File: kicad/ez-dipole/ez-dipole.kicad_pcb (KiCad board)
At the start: 2 copper layers, 200 x 80 mm, 4 parts, among them J1 Conn_Coaxial

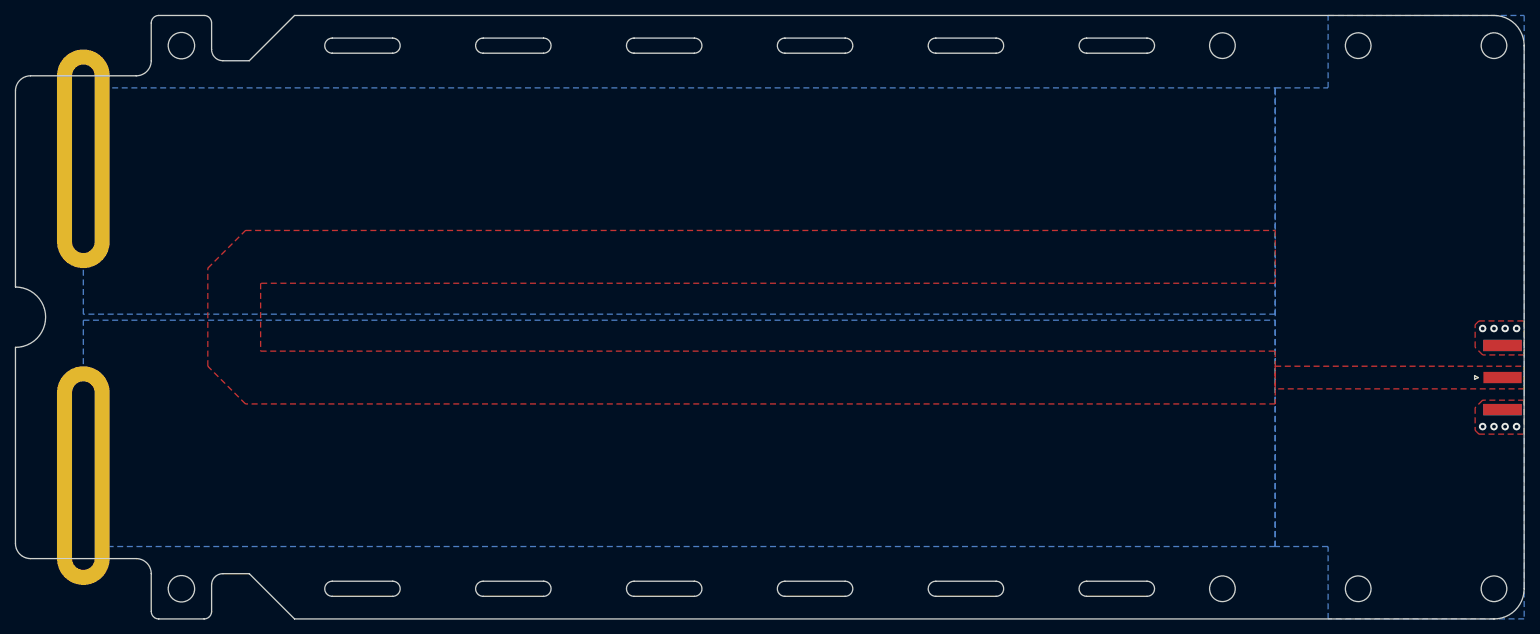
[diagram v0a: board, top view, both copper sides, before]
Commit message: Increased slot length outside of board outline and adapted SMA footprint to allow also smaller SMA connectors
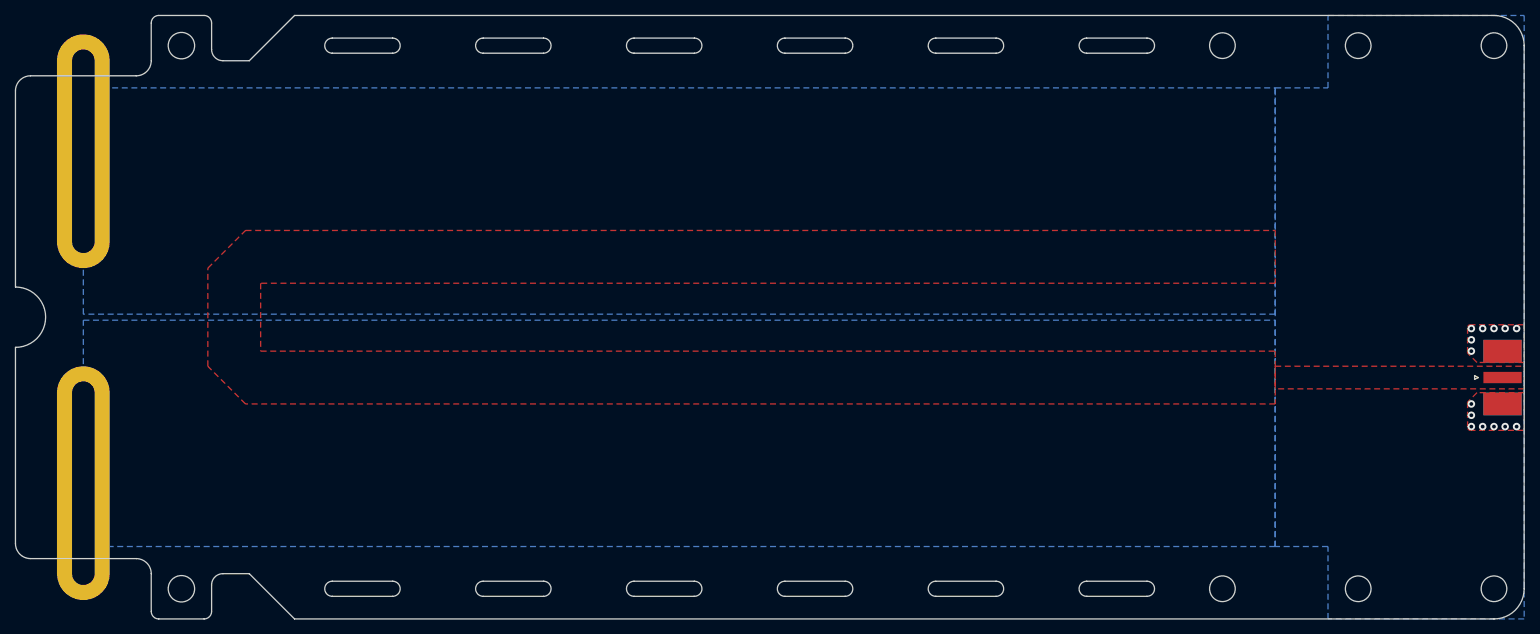
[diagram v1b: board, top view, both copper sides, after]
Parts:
- J1: footprint Connector_Coaxial:SMA_Amphenol_132289_EdgeMount -> ez-dipole:SMA_Amphenol_132289_EdgeMount
- moved TP1 1.00 mm to (60.0, 68.0)
- moved TP2 1.00 mm to (60.0, 112.0)
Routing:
- net GND: vias 8 -> 14
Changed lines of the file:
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@@
   (net 2 "/HOT")
   (footprint "ez-dipole:Slot" (layer "F.Cu")
-    (at 60 111 90)
+    (at 60 112 90)
     (property "Sheetfile" "ez-dipole.kicad_sch")
     (property "Sheetname" "")
@@
       (effects (font (size 1 1) (thickness 0.15)))
     )
-    (pad "1" thru_hole oval (at 0 0 90) (size 29 7) (drill oval 25 3) (layers *.Cu *.Mask)
+    (pad "1" thru_hole oval (at 0 0 90) (size 31 7) (drill oval 27 3) (layers *.Cu *.Mask)
       (net 1 "GND") (pinfunction "1") (pintype "passive"))
   )
-  (footprint "Connector_Coaxial:SMA_Amphenol_132289_EdgeMount" (layer "F.Cu")
+  (footprint "ez-dipole:SMA_Amphenol_132289_EdgeMount" locked (layer "F.Cu")
     (at 248.1375 98)
     (descr "http://www.amphenolrf.com/132289.html")
@@
       (effects (font (size 1 1) (thickness 0.15)))
     )
-    (fp_text value "Conn_Coaxial" (at 5 6) (layer "F.Fab") hide
+    (fp_text value "Conn_Coaxial" (at 5 6) (layer "F.Fab")
       (effects (font (size 1 1) (thickness 0.15)))
     )
-    (fp_text user "${REFERENCE}" (at 4.79 0 270) (layer "F.Fab") hide
+    (fp_text user "${REFERENCE}" (at 4.79 0 270) (layer "F.Fab")
       (effects (font (size 1 1) (thickness 0.15)))
     )
+    (fp_line (start -3.71 0.25) (end -3.21 0) (layer "F.SilkS") (width 0.12))
+    (fp_line (start -3.21 0) (end -3.71 -0.25) (layer "F.SilkS") (width 0.12))
     (fp_line (start -3.71 -0.25) (end -3.71 0.25) (layer "F.SilkS") (width 0.12))
-    (fp_line (start -3.21 0) (end -3.71 -0.25) (layer "F.SilkS") (width 0.12))
-    (fp_line (start -3.71 0.25) (end -3.21 0) (layer "F.SilkS") (width 0.12))
-    (fp_line (start 14.47 -5.58) (end -3.04 -5.58) (layer "B.CrtYd") (width 0.05))
+    (fp_line (start -3.04 5.58) (end -3.04 -5.58) (layer "B.CrtYd") (width 0.05))
     (fp_line (start 14.47 -5.58) (end 14.47 5.58) (layer "B.CrtYd") (width 0.05))
     (fp_line (start 14.47 5.58) (end -3.04 5.58) (layer "B.CrtYd") (width 0.05))
-    (fp_line (start -3.04 5.58) (end -3.04 -5.58) (layer "B.CrtYd") (width 0.05))
+    (fp_line (start 14.47 -5.58) (end -3.04 -5.58) (layer "B.CrtYd") (width 0.05))
     (fp_line (start 14.47 5.58) (end -3.04 5.58) (layer "F.CrtYd") (width 0.05))
     (fp_line (start 14.47 -5.58) (end 14.47 5.58) (layer "F.CrtYd") (width 0.05))
@@
     (fp_line (start 14.47 -5.58) (end -3.04 -5.58) (layer "F.CrtYd") (width 0.05))
     (fp_line (start 2.54 3.81) (end -1.91 3.81) (layer "F.Fab") (width 0.1))
-    (fp_line (start 2.54 -3.81) (end 2.54 3.81) (layer "F.Fab") (width 0.1))
-    (fp_line (start -1.91 -5.08) (end 4.445 -5.08) (layer "F.Fab") (width 0.1))
     (fp_line (start 4.445 -3.81) (end 13.97 -3.81) (layer "F.Fab") (width 0.1))
     (fp_line (start 3.54 0) (end 2.54 0.75) (layer "F.Fab") (width 0.1))
+    (fp_line (start 13.97 -3.81) (end 13.97 3.81) (layer "F.Fab") (width 0.1))
+    (fp_line (start 4.445 5.08) (end 4.445 3.81) (layer "F.Fab") (width 0.1))
+    (fp_line (start 2.54 -3.81) (end 2.54 3.81) (layer "F.Fab") (width 0.1))
     (fp_line (start -1.91 3.81) (end -1.91 5.08) (layer "F.Fab") (width 0.1))
+    (fp_line (start -1.91 -5.08) (end 4.445 -5.08) (layer "F.Fab") (width 0.1))
+    (fp_line (start 2.54 -0.75) (end 3.54 0) (layer "F.Fab") (width 0.1))
+    (fp_line (start -1.91 -3.81) (end 2.54 -3.81) (layer "F.Fab") (width 0.1))
     (fp_line (start -1.91 -5.08) (end -1.91 -3.81) (layer "F.Fab") (width 0.1))
+    (fp_line (start -1.91 5.08) (end 4.445 5.08) (layer "F.Fab") (width 0.1))
+    (fp_line (start 4.445 -3.81) (end 4.445 -5.08) (layer "F.Fab") (width 0.1))
     (fp_line (start 13.97 3.81) (end 4.445 3.81) (layer "F.Fab") (width 0.1))
-    (fp_line (start 2.54 -0.75) (end 3.54 0) (layer "F.Fab") (width 0.1))
-    (fp_line (start 4.445 -3.81) (end 4.445 -5.08) (layer "F.Fab") (width 0.1))
-    (fp_line (start -1.91 -3.81) (end 2.54 -3.81) (layer "F.Fab") (width 0.1))
-    (fp_line (start 4.445 5.08) (end 4.445 3.81) (layer "F.Fab") (width 0.1))
-    (fp_line (start -1.91 5.08) (end 4.445 5.08) (layer "F.Fab") (width 0.1))
-    (fp_line (start 13.97 -3.81) (end 13.97 3.81) (layer "F.Fab") (width 0.1))
-    (pad "1" smd rect (at 0 0 90) (size 1.5 5.08) (layers "F.Cu" "F.Paste" "F.Mask")
+    (pad "1" smd rect locked (at 0 0 90) (size 1.5 5.08) (layers "F.Cu" "F.Paste" "F.Mask")
       (net 2 "/HOT") (pinfunction "In") (pintype "passive"))
-    (pad "2" smd rect (at 0 4.25 90) (size 1.5 5.08) (layers "B.Cu" "B.Paste" "B.Mask")
+    (pad "2" smd rect locked (at 0 3.5 90) (size 3 5.08) (layers "F.Cu" "F.Paste" "F.Mask")
       (net 1 "GND") (pinfunction "Ext") (pintype "passive"))
-    (pad "2" smd rect (at 0 4.25 90) (size 1.5 5.08) (layers "F.Cu" "F.Paste" "F.Mask")
+    (pad "2" smd rect locked (at 0 -3.5 90) (size 3 5.08) (layers "B.Cu" "B.Paste" "B.Mask")
       (net 1 "GND") (pinfunction "Ext") (pintype "passive"))
-    (pad "2" smd rect (at 0 -4.25 90) (size 1.5 5.08) (layers "B.Cu" "B.Paste" "B.Mask")
+    (pad "2" smd rect locked (at 0 -3.5 90) (size 3 5.08) (layers "F.Cu" "F.Paste" "F.Mask")
       (net 1 "GND") (pinfunction "Ext") (pintype "passive"))
-    (pad "2" smd rect (at 0 -4.25 90) (size 1.5 5.08) (layers "F.Cu" "F.Paste" "F.Mask")
+    (pad "2" smd rect locked (at 0 3.5 90) (size 3 5.08) (layers "B.Cu" "B.Paste" "B.Mask")
       (net 1 "GND") (pinfunction "Ext") (pintype "passive"))
     (model "${KIPRJMOD}/../library/ez-dipole.3dshapes/SMA_Amphenol_132289_EdgeMount.stp"
-      (offset (xyz 2.9 0 0.4))
+      (offset (xyz 2.5 0 0.35))
       (scale (xyz 1 1 1))
-      (rotate (xyz 90 -180 0))
+      (rotate (xyz -90 0 180))
     )
   )
   (footprint "ez-dipole:Slot" (layer "F.Cu")
-    (at 60 69 90)
+    (at 60 68 90)
     (property "Sheetfile" "ez-dipole.kicad_sch")
     (property "Sheetname" "")
@@
       (effects (font (size 1 1) (thickness 0.15)))
     )
-    (pad "1" thru_hole oval (at 0 0 90) (size 29 7) (drill oval 25 3) (layers *.Cu *.Mask)
+    (pad "1" thru_hole oval (at 0 0 90) (size 31 7) (drill oval 27 3) (layers *.Cu *.Mask)
       (net 1 "GND") (pinfunction "1") (pintype "passive"))
   )
@@
   (gr_rect (start 251 130) (end 51 122) (layer "B.Mask") (width 0.15) (fill solid))
   (gr_rect (start 251 58) (end 51 50) (layer "F.Mask") (width 0.15) (fill solid))
+  (gr_rect (start 250.7 93) (end 245.6 96) (layer "F.Mask") (width 0.1) (fill solid))
+  (gr_rect (start 245.6 103) (end 250.7 100) (layer "F.Mask") (width 0.1) (fill solid))
   (gr_rect (start 251 130) (end 51 122) (layer "F.Mask") (width 0.15) (fill solid))
   (gr_line (start 250 90) (end 50 90) (layer "Dwgs.User") (width 0.15))
@@
   )
   (via (at 247 91.5) (size 1) (drill 0.5) (layers "F.Cu" "B.Cu") (free) (net 1))
+  (via (at 248.478731 104.501145) (size 1) (drill 0.5) (layers "F.Cu" "B.Cu") (free) (net 1))
+  (via (at 250 104.5) (size 1) (drill 0.5) (layers "F.Cu" "B.Cu") (free) (net 1))
+  (via (at 244 104.5) (size 1) (drill 0.5) (layers "F.Cu" "B.Cu") (free) (net 1))
   (via (at 250 91.5) (size 1) (drill 0.5) (layers "F.Cu" "B.Cu") (free) (net 1))
-  (via (at 250 104.5) (size 1) (drill 0.5) (layers "F.Cu" "B.Cu") (free) (net 1))
+  (via (at 245.5 104.5) (size 1) (drill 0.5) (layers "F.Cu" "B.Cu") (free) (net 1))
   (via (at 248.478731 91.498855) (size 1) (drill 0.5) (layers "F.Cu" "B.Cu") (free) (net 1))
+  (via (at 244 91.5) (size 1) (drill 0.5) (layers "F.Cu" "B.Cu") (free) (net 1))
+  (via (at 244 103) (size 1) (drill 0.5) (layers "F.Cu" "B.Cu") (free) (net 1))
+  (via (at 244 93) (size 1) (drill 0.5) (layers "F.Cu" "B.Cu") (free) (net 1))
   (via (at 247 104.5) (size 1) (drill 0.5) (layers "F.Cu" "B.Cu") (free) (net 1))
-  (via (at 248.478731 104.501145) (size 1) (drill 0.5) (layers "F.Cu" "B.Cu") (free) (net 1))
+  (via (at 244 94.5) (size 1) (drill 0.5) (layers "F.Cu" "B.Cu") (free) (net 1))
   (via (at 245.5 91.5) (size 1) (drill 0.5) (layers "F.Cu" "B.Cu") (free) (net 1))
-  (via (at 245.5 104.5) (size 1) (drill 0.5) (layers "F.Cu" "B.Cu") (free) (net 1))
+  (via (at 244 101.5) (size 1) (drill 0.5) (layers "F.Cu" "B.Cu") (free) (net 1))
   (zone (net 2) (net_name "/HOT") (layer "F.Cu") (hatch edge 0.508)
     (connect_pads yes (clearance 0.508))
@@
     )
   )
+  (zone (net 1) (net_name "GND") (layer "F.Cu") (hatch edge 0.508)
+    (connect_pads yes (clearance 0.3))
+    (min_thickness 0.254) (filled_areas_thickness no)
+    (fill yes (thermal_gap 0.508) (thermal_bridge_width 0.508) (island_removal_mode 1) (island_area_min 0))
+    (polygon
+      (pts
+        (xy 251 100)
+        (xy 244.75 100)
+        (xy 243.5 101.25)
+        (xy 243.5 104.75)
+        (xy 243.75 105)
+        (xy 251 105)
+      )
+    )
+  )
   (zone (net 2) (net_name "/HOT") (layer "F.Cu") (hatch edge 0.508)
     (connect_pads yes (clearance 0.3))
@@
     (polygon
       (pts
-        (xy 251 95)
-        (xy 245.5 95)
-        (xy 244.5 94)
-        (xy 244.5 91)
-        (xy 245 90.5)
-        (xy 251 90.5)
+        (xy 251 96)
+        (xy 244.75 96)
+        (xy 243.5 94.75)
+        (xy 243.5 91.25)
+        (xy 243.75 91)
+        (xy 251 91)
       )
     )
-  )
-  (zone (net 1) (net_name "GND") (layer "F.Cu") (hatch edge 0.508)
-    (connect_pads yes (clearance 0.3))
-    (min_thickness 0.254) (filled_areas_thickness no)
-    (fill yes (thermal_gap 0.508) (thermal_bridge_width 0.508) (island_removal_mode 1) (island_area_min 0))
-    (polygon
-      (pts
-        (xy 251 101)
-        (xy 245.5 101)
-        (xy 244.5 102)
-        (xy 244.5 105)
-        (xy 245 105.5)
-        (xy 251 105.5)
-      )
-    )

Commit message: Updated PCB to revision 1.1 with updated simulation data
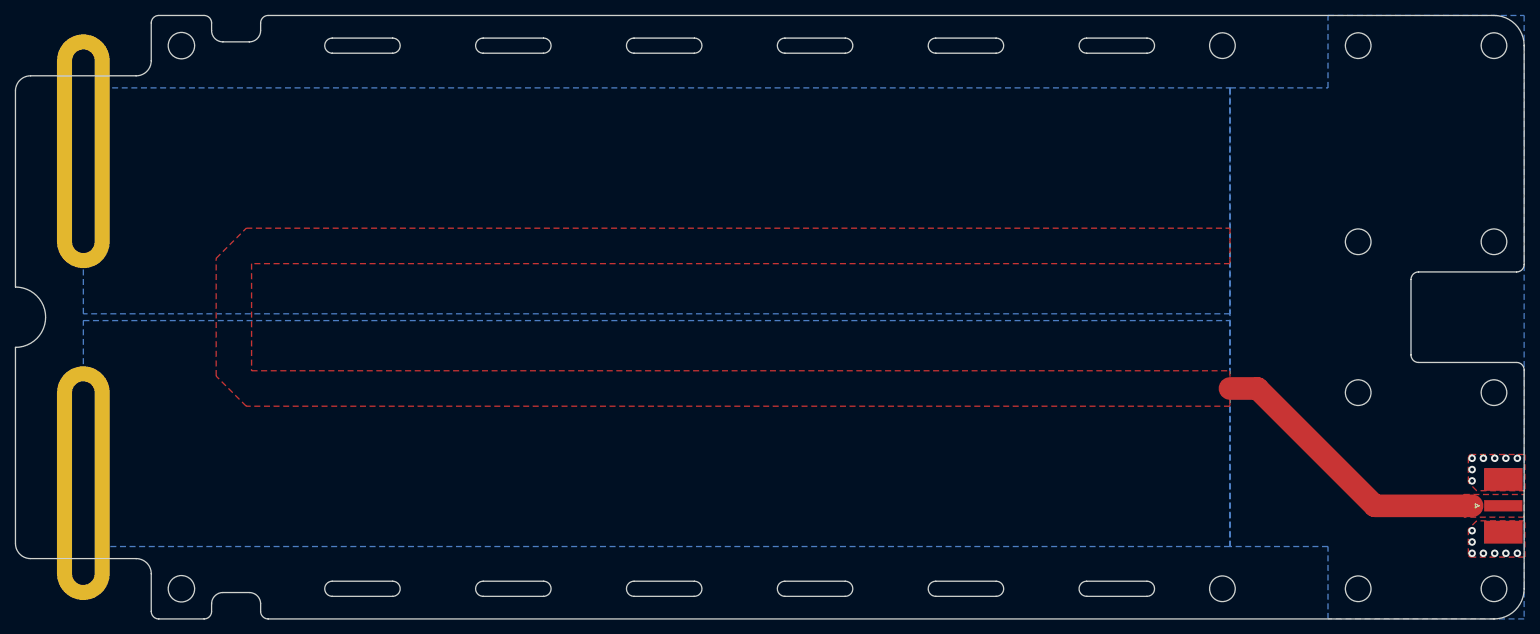
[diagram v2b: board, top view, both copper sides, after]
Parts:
- moved REF** 37.7 mm to (236.7, 69.9), turned to 0 degrees
- moved J1 17.0 mm to (248.2, 115.0)
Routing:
- net /HOT: track 0.00 -> 38.5 mm
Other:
- outline, holes or cut-outs redrawn
- board text added: "EZ-Dipole V1.1 S. Kueppers"
- board text removed: "EZ-Dipole V1.0 S. Kueppers"
